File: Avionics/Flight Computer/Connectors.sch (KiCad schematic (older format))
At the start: 3 parts, among them J1 ERF8-040-05.0-S-DV-K, J2 ERF8-040-05.0-S-DV-K, J3 473460001

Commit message: Nearly completed initial placement.
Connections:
- net VUSB: now reaches J3.1 (VBUS)
- net USBD_N: now reaches J3.2 (D-)
- net USBD_P: now reaches J3.3 (D+)
- net GND: now reaches J3.5 (GND)
- net GND: now also J3.6 (Shield)
- no-connect marks 0 -> 1
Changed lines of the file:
@@
 	1    0    0    -1
 $EndComp
+$Comp
+L VUSB #PWR0110
+U 1 1 58B8BBBA
+P 1600 1150
+F 0 "#PWR0110" H -400 -250 50  0001 C CNN
+F 1 "VUSB" H 1615 1323 50  0000 C CNN
+F 2 "" H -400 -100 50  0001 C CNN
+F 3 "" H -400 -100 50  0001 C CNN
+	1    1600 1150
+	1    0    0    -1
+$EndComp
+Wire Wire Line
+	1500 1250 1600 1250
+Wire Wire Line
+	1600 1250 1600 1150
+$Comp
+L GND #PWR0111
+U 1 1 58B8BD69
+P 1100 1900
+F 0 "#PWR0111" H -800 50  50  0001 C CNN
+F 1 "GND" H 1105 1727 50  0000 C CNN
+F 2 "" H -800 300 50  0001 C CNN
+F 3 "" H -800 300 50  0001 C CNN
+	1    1100 1900
+	1    0    0    -1
+$EndComp
+Wire Wire Line
+	1100 1900 1100 1850
+Wire Wire Line
+	1100 1850 1200 1850
+NoConn ~ 1500 1650
+Wire Wire Line
+	1500 1450 1800 1450
+Wire Wire Line
+	1500 1550 1800 1550
+Text HLabel 1800 1450 2    60   BiDi ~ 0
+USBD_P
+Text HLabel 1800 1550 2    60   BiDi ~ 0
+USBD_N
 $EndSCHEMATC

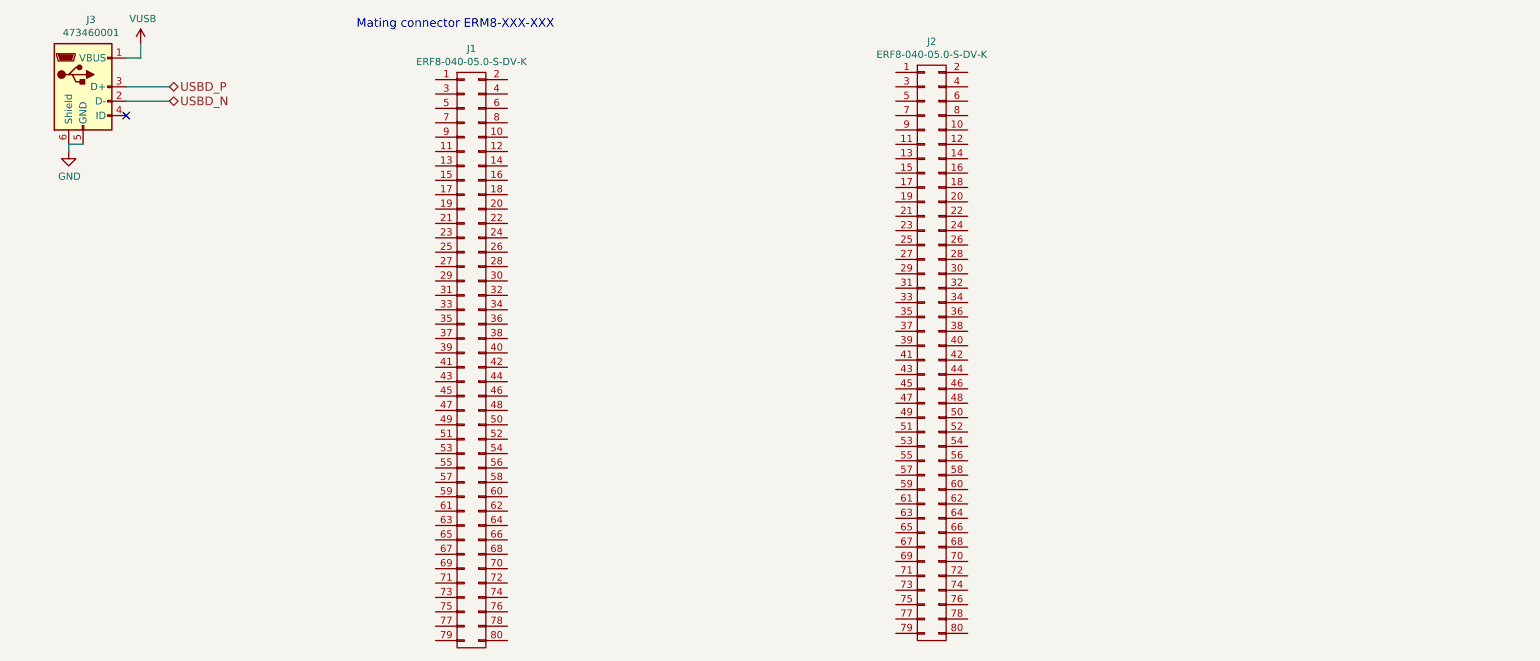
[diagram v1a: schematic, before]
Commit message: Wired up everything and started rearranging layout
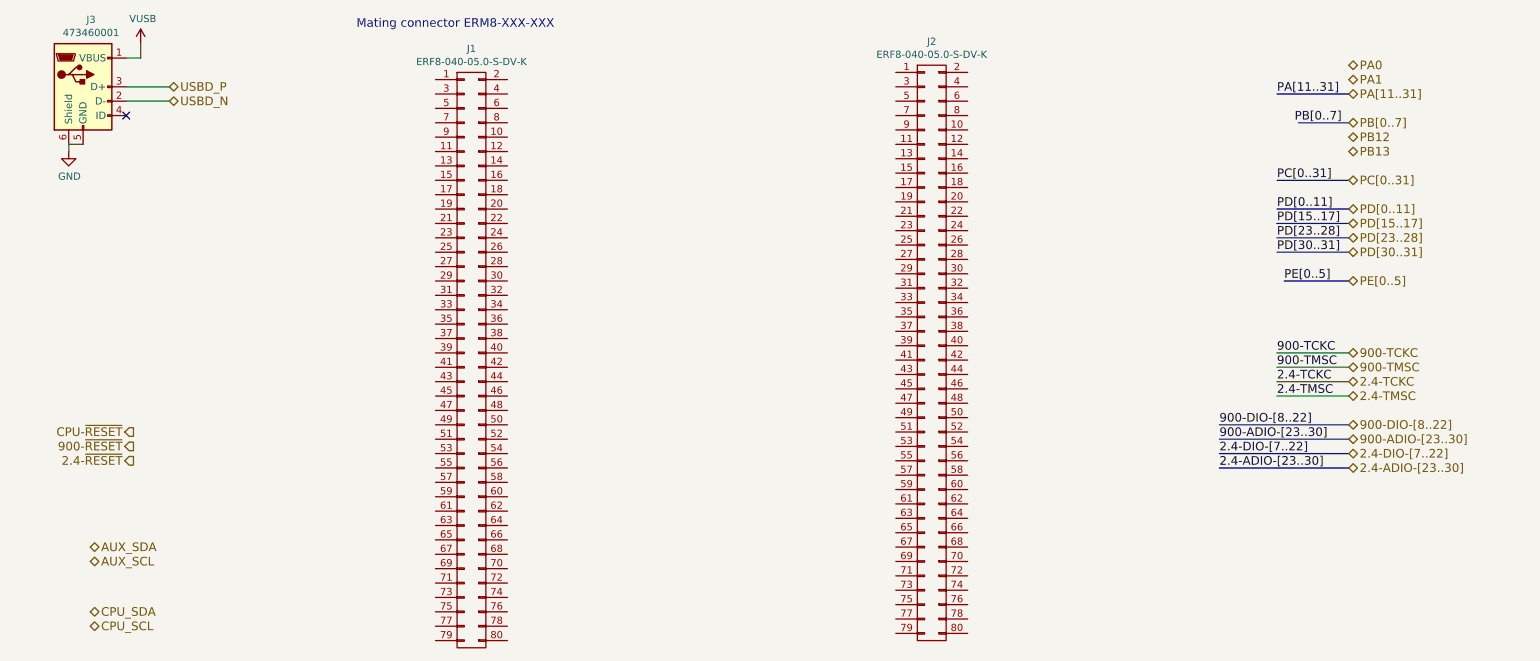
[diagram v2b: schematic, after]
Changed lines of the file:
@@
 $Descr A4 11693 8268
 encoding utf-8
-Sheet 9 9
+Sheet 8 8
 Title ""
 Date ""
@@
 $EndComp
 $Comp
-L VUSB #PWR0110
+L VUSB #PWR0107
 U 1 1 58B8BBBA
 P 1600 1150
-F 0 "#PWR0110" H -400 -250 50  0001 C CNN
+F 0 "#PWR0107" H -400 -250 50  0001 C CNN
 F 1 "VUSB" H 1615 1323 50  0000 C CNN
 F 2 "" H -400 -100 50  0001 C CNN
@@
 	1600 1250 1600 1150
 $Comp
-L GND #PWR0111
+L GND #PWR0108
 U 1 1 58B8BD69
 P 1100 1900
-F 0 "#PWR0111" H -800 50  50  0001 C CNN
+F 0 "#PWR0108" H -800 50  50  0001 C CNN
 F 1 "GND" H 1105 1727 50  0000 C CNN
 F 2 "" H -800 300 50  0001 C CNN
@@
 Text HLabel 1800 1550 2    60   BiDi ~ 0
 USBD_N
+Text HLabel 1550 3850 0    60   Output ~ 0
+CPU-~RESET
+Text HLabel 1550 3950 0    60   Output ~ 0
+900-~RESET
+Text HLabel 1550 4050 0    60   Output ~ 0
+2.4-~RESET
+Text HLabel 10000 2100 2    60   BiDi ~ 0
+PC[0..31]
+Wire Bus Line
+	10000 2100 9500 2100
+Text Label 9500 2100 0    60   ~ 0
+PC[0..31]
+Text HLabel 10000 2300 2    60   BiDi ~ 0
+PD[0..11]
+Wire Bus Line
+	10000 2300 9500 2300
+Text Label 9500 2300 0    60   ~ 0
+PD[0..11]
+Text HLabel 10000 2400 2    60   BiDi ~ 0
+PD[15..17]
+Wire Bus Line
+	10000 2400 9500 2400
+Text Label 9500 2400 0    60   ~ 0
+PD[15..17]
+Text HLabel 10000 2500 2    60   BiDi ~ 0
+PD[23..28]
+Wire Bus Line
+	10000 2500 9500 2500
+Text Label 9500 2500 0    60   ~ 0
+PD[23..28]
+Text HLabel 10000 2800 2    60   BiDi ~ 0
+PE[0..5]
+Wire Bus Line
+	10000 2800 9550 2800
+Text Label 9550 2800 0    60   ~ 0
+PE[0..5]
+Text Label 9500 2600 0    60   ~ 0
+PD[30..31]
+Text HLabel 10000 2600 2    60   BiDi ~ 0
+PD[30..31]
+Wire Bus Line
+	9500 2600 10000 2600
+Text HLabel 1250 4650 2    60   BiDi ~ 0
+AUX_SDA
+Text HLabel 1250 4750 2    60   BiDi ~ 0
+AUX_SCL
+Text HLabel 1250 5100 2    60   BiDi ~ 0
+CPU_SDA
+Text HLabel 1250 5200 2    60   BiDi ~ 0
+CPU_SCL
+Text HLabel 10000 1500 2    60   BiDi ~ 0
+PA[11..31]
+Wire Bus Line
+	10000 1500 9500 1500
+Text Label 9500 1500 0    60   ~ 0
+PA[11..31]
+Text HLabel 10000 1300 2    60   BiDi ~ 0
+PA0
+Text HLabel 10000 1400 2    60   BiDi ~ 0
+PA1
+Text HLabel 10000 1700 2    60   BiDi ~ 0
+PB[0..7]
+Text HLabel 10000 1900 2    60   BiDi ~ 0
+PB13
+Text HLabel 10000 1800 2    60   BiDi ~ 0
+PB12
+Wire Bus Line
+	10000 1700 9650 1700
+Text Label 9950 1700 2    60   ~ 0
+PB[0..7]
+Wire Wire Line
+	10000 3300 9500 3300
+Wire Wire Line
+	10000 3400 9500 3400
+Text Label 9500 3300 0    60   ~ 0
+900-TCKC
+Text Label 9500 3400 0    60   ~ 0
+900-TMSC
+Wire Wire Line
+	10000 3500 9500 3500
+Text Label 9500 3500 0    60   ~ 0
+2.4-TCKC
+Text Label 9500 3600 0    60   ~ 0
+2.4-TMSC
+Wire Wire Line
+	9500 3600 10000 3600
+Text HLabel 10000 3300 2    60   BiDi ~ 0
+900-TCKC
+Text HLabel 10000 3400 2    60   BiDi ~ 0
+900-TMSC
+Text HLabel 10000 3500 2    60   BiDi ~ 0
+2.4-TCKC
+Text HLabel 10000 3600 2    60   BiDi ~ 0
+2.4-TMSC
+Wire Bus Line
+	9100 3800 10000 3800
+Wire Bus Line
+	9100 3900 10000 3900
+Text Label 9100 3900 0    60   ~ 0
+900-ADIO-[23..30]
+Text Label 9100 3800 0    60   ~ 0
+900-DIO-[8..22]
+Wire Bus Line
+	9100 4000 10000 4000
+Wire Bus Line
+	9100 4100 10000 4100
+Text Label 9100 4100 0    60   ~ 0
+2.4-ADIO-[23..30]
+Text Label 9100 4000 0    60   ~ 0
+2.4-DIO-[7..22]
+Text HLabel 10000 3800 2    60   BiDi ~ 0
+900-DIO-[8..22]
+Text HLabel 10000 3900 2    60   BiDi ~ 0
+900-ADIO-[23..30]
+Text HLabel 10000 4000 2    60   BiDi ~ 0
+2.4-DIO-[7..22]
+Text HLabel 10000 4100 2    60   BiDi ~ 0
+2.4-ADIO-[23..30]
 $EndSCHEMATC

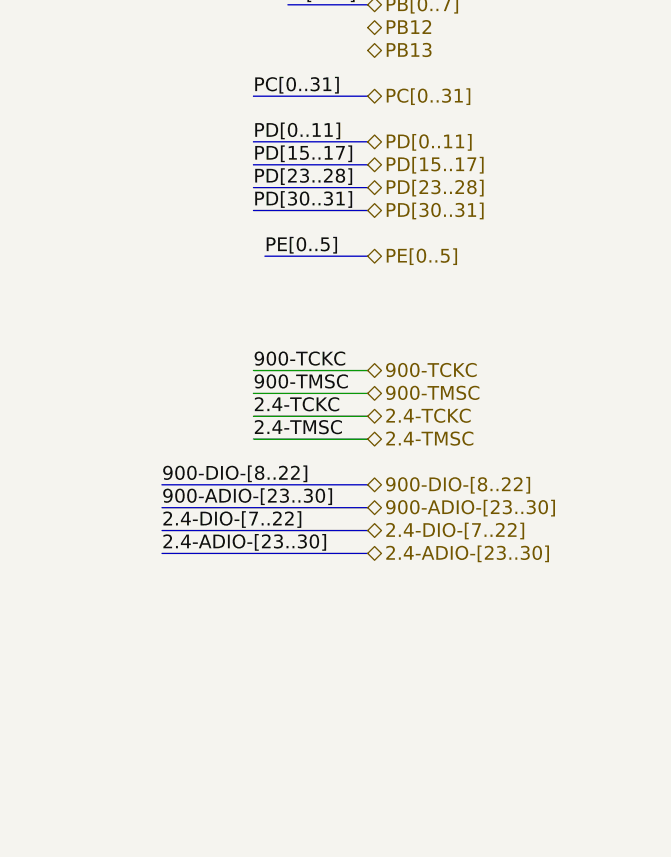
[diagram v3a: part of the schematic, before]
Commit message: Fixed missing connections and did more layout
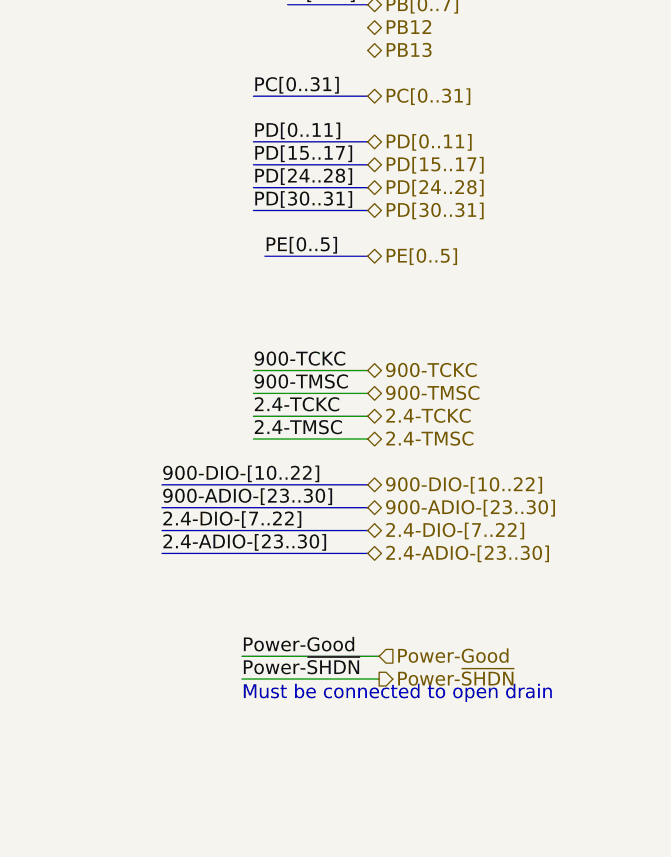
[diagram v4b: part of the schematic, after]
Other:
- note added: "Must be connected to open drain\n"
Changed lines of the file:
@@
 PD[15..17]
 Text HLabel 10000 2500 2    60   BiDi ~ 0
-PD[23..28]
+PD[24..28]
 Wire Bus Line
 	10000 2500 9500 2500
 Text Label 9500 2500 0    60   ~ 0
-PD[23..28]
+PD[24..28]
 Text HLabel 10000 2800 2    60   BiDi ~ 0
 PE[0..5]
@@
 900-ADIO-[23..30]
 Text Label 9100 3800 0    60   ~ 0
-900-DIO-[8..22]
+900-DIO-[10..22]
 Wire Bus Line
 	9100 4000 10000 4000
@@
 2.4-DIO-[7..22]
 Text HLabel 10000 3800 2    60   BiDi ~ 0
-900-DIO-[8..22]
+900-DIO-[10..22]
 Text HLabel 10000 3900 2    60   BiDi ~ 0
 900-ADIO-[23..30]
@@
 Text HLabel 10000 4100 2    60   BiDi ~ 0
 2.4-ADIO-[23..30]
+Wire Wire Line
+	9450 4550 10050 4550
+Text Label 9450 4550 0    60   ~ 0
+Power-Good
+Text HLabel 10050 4550 2    60   Input ~ 0
+Power-Good
+Text Label 9450 4650 0    60   ~ 0
+Power-~SHDN
+Text HLabel 10050 4650 2    60   Output ~ 0
+Power-~SHDN
+Wire Wire Line
+	9450 4650 10050 4650
+Text Notes 9450 4750 0    60   ~ 0
+Must be connected to open drain\n
 $EndSCHEMATC

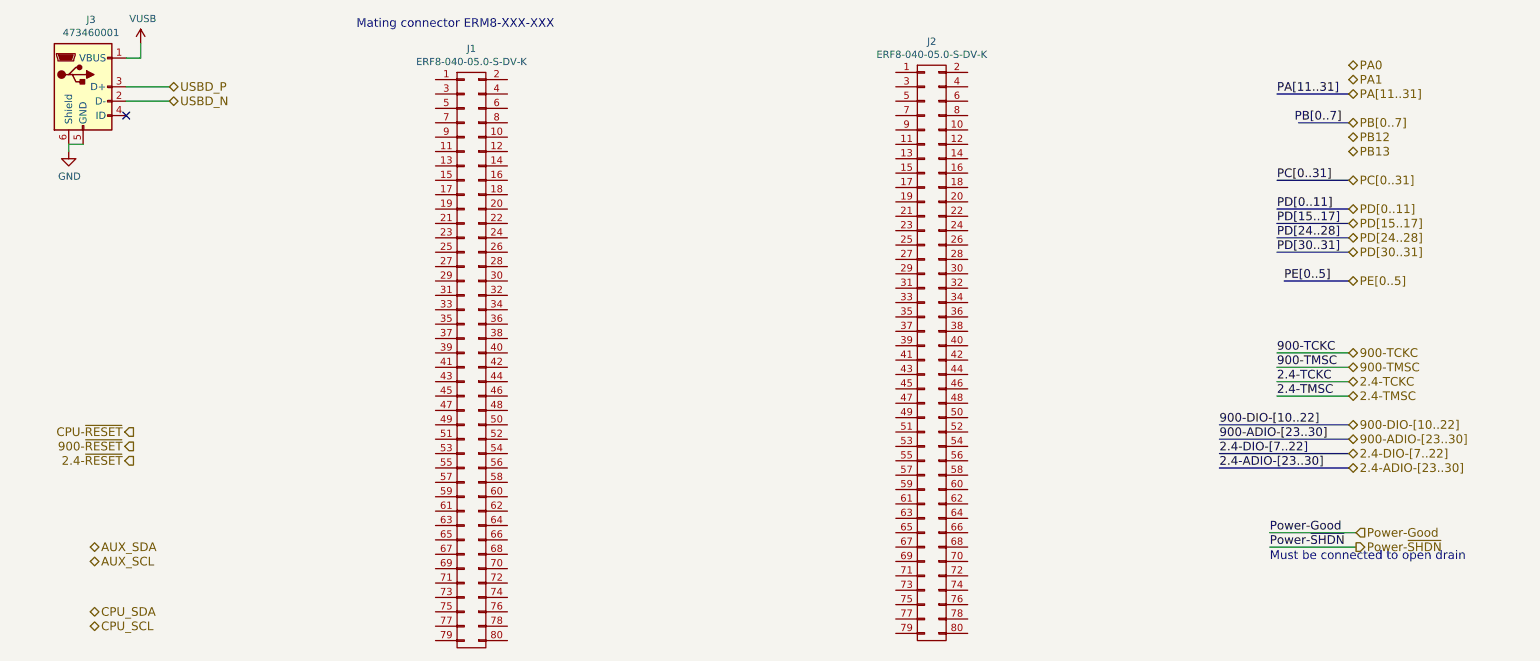
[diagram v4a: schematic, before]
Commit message: Some more pin swapping and routing of signals. Placed reset pullup resistors.
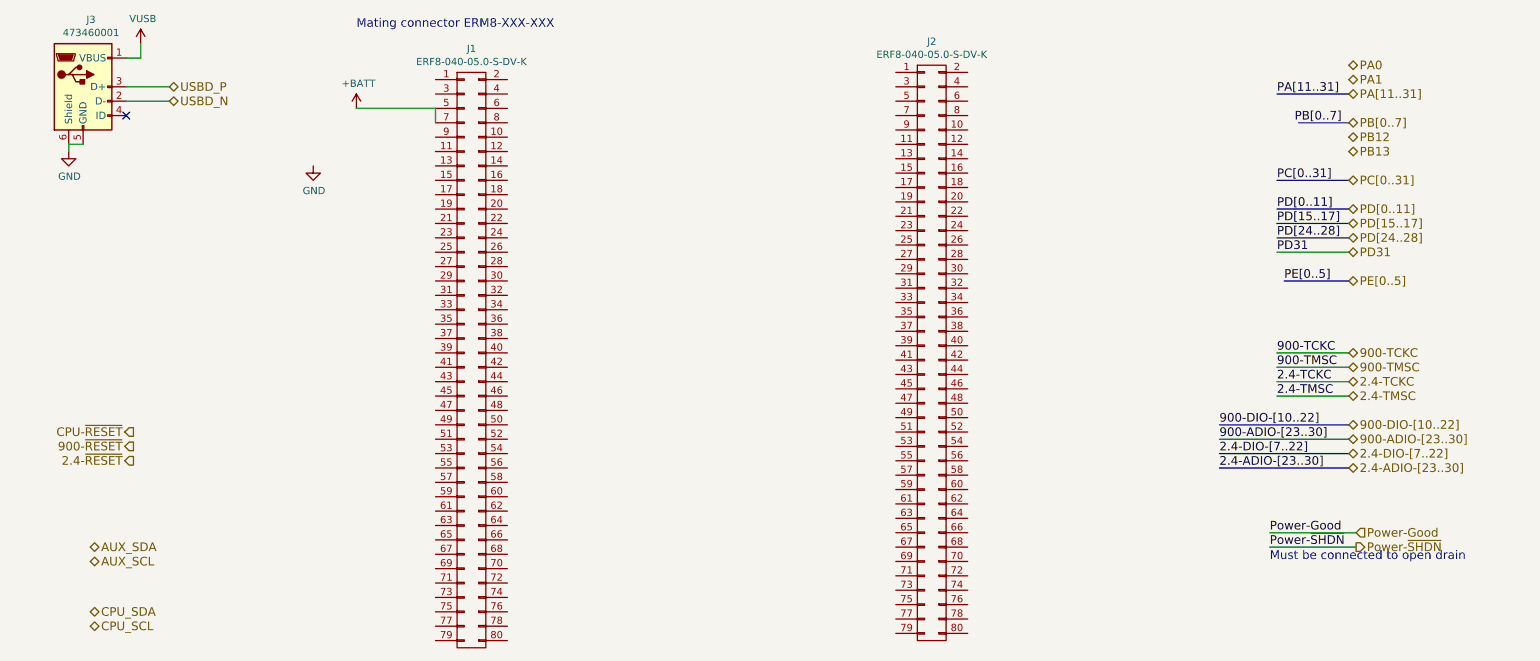
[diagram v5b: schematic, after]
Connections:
- net +BATT: now reaches J1.5 (P5)
- net +BATT: now also J1.7 (P7)
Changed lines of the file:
@@
 $EndComp
 $Comp
-L VUSB #PWR0114
+L VUSB #PWR117
 U 1 1 58B8BBBA
 P 1600 1150
-F 0 "#PWR0114" H -400 -250 50  0001 C CNN
+F 0 "#PWR117" H -400 -250 50  0001 C CNN
 F 1 "VUSB" H 1615 1323 50  0000 C CNN
 F 2 "" H -400 -100 50  0001 C CNN
@@
 	1600 1250 1600 1150
 $Comp
-L GND #PWR0115
+L GND #PWR116
 U 1 1 58B8BD69
 P 1100 1900
-F 0 "#PWR0115" H -800 50  50  0001 C CNN
+F 0 "#PWR116" H -800 50  50  0001 C CNN
 F 1 "GND" H 1105 1727 50  0000 C CNN
 F 2 "" H -800 300 50  0001 C CNN
@@
 PE[0..5]
 Text Label 9500 2600 0    60   ~ 0
-PD[30..31]
+PD31
 Text HLabel 10000 2600 2    60   BiDi ~ 0
-PD[30..31]
-Wire Bus Line
-	9500 2600 10000 2600
+PD31
 Text HLabel 1250 4650 2    60   BiDi ~ 0
 AUX_SDA
@@
 Text Notes 9450 4750 0    60   ~ 0
 Must be connected to open drain\n
+Wire Wire Line
+	3100 1600 3650 1600
+$Comp
+L +BATT #PWR118
+U 1 1 58DB91A4
+P 3100 1600
+F 0 "#PWR118" H 2050 -1300 50  0001 C CNN
+F 1 "+BATT" H 3115 1773 50  0000 C CNN
+F 2 "" H 2050 -1150 50  0001 C CNN
+F 3 "" H 2050 -1150 50  0001 C CNN
+	1    3100 1600
+	1    0    0    -1
+$EndComp
+Wire Wire Line
+	3650 1600 3650 1700
+Wire Wire Line
+	9500 2600 10000 2600
+$Comp
+L GND #PWR?
+U 1 1 58DD26EA
+P 2800 2000
+F 0 "#PWR?" H -1150 -1700 50  0001 C CNN
+F 1 "GND" H 2805 1827 50  0000 C CNN
+F 2 "" H -1150 -1450 50  0001 C CNN
+F 3 "" H -1150 -1450 50  0001 C CNN
+	1    2800 2000
+	1    0    0    -1
+$EndComp
 $EndSCHEMATC
